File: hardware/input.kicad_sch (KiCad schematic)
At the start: 5 parts, among them J5 Conn_Coaxial

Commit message: FEM v3 Updates
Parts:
- C105: value 100n -> 470n; footprint Capacitor_SMD:C_0402_1005Metric -> Capacitor_SMD:C_0603_1608Metric; LCSC C60474 -> C1623; MPN CC0402KRX7R7BB104 -> CL10B474KA8NNNC
- L25, L6: value 150u -> 47u; footprint Inductor_SMD:L_1812_4532Metric -> Inductor_SMD:L_0603_1608Metric; LCSC C394135 -> C2844630; MPN FHW1812IF151JST -> MLW1608RF-470MT

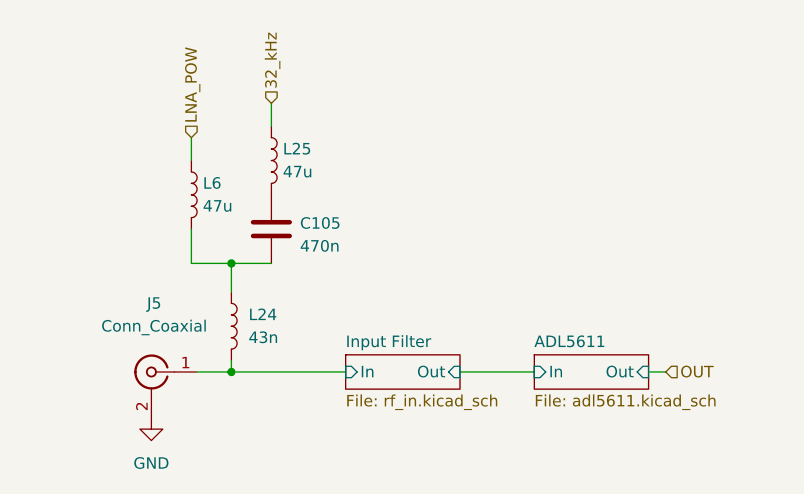
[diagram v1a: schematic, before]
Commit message: Remove cal circuit, swap attens, swap norflash
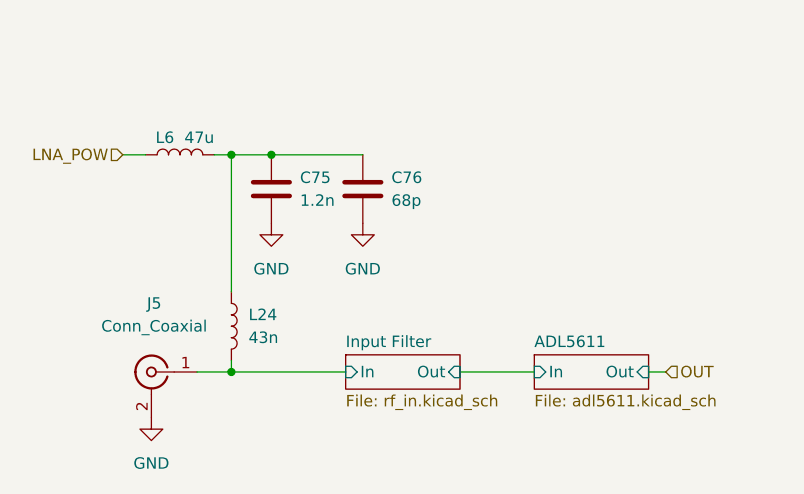
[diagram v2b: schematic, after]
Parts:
- removed C105: 470n, Capacitor_SMD:C_0603_1608Metric, symbol Device:C
- removed L25: 47u, Inductor_SMD:L_0603_1608Metric, symbol Device:L
- added C75: 1.2n, Capacitor_SMD:C_0603_1608Metric, symbol Device:C
- added C76: 68p, Capacitor_SMD:C_0603_1608Metric, symbol Device:C
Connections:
- net GND: now also C75.1, C76.1
- net at L24.1, L6.2: now also C75.2, C76.2
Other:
- moved on the sheet: L6

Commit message: Update FEM hardware design for production version
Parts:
- renumbered J5 to J6, L6 to L22, L24 to L23
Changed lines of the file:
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@@
         )
         (path "/e63e39d7-6ac0-4ffd-8aa3-1841a4541b55/546148dc-8a5c-4178-ace4-1d6889891417/a017f007-4f07-4a1d-ad0a-a026b6928c1c"
-          (reference "#PWR04") (unit 1)
+          (reference "#PWR083") (unit 1)
         )
       )
@@
         )
         (path "/e63e39d7-6ac0-4ffd-8aa3-1841a4541b55/546148dc-8a5c-4178-ace4-1d6889891417/b519df87-7202-4a5b-9b12-1283a4d92d20"
-          (reference "C33") (unit 1)
-        )
-        (path "/e63e39d7-6ac0-4ffd-8aa3-1841a4541b55/546148dc-8a5c-4178-ace4-1d6889891417/a017f007-4f07-4a1d-ad0a-a026b6928c1c"
-          (reference "C102") (unit 1)
+          (reference "C2") (unit 1)
+        )
+        (path "/e63e39d7-6ac0-4ffd-8aa3-1841a4541b55/546148dc-8a5c-4178-ace4-1d6889891417/a017f007-4f07-4a1d-ad0a-a026b6928c1c"
+          (reference "C53") (unit 1)
         )
       )
@@
         )
         (path "/e63e39d7-6ac0-4ffd-8aa3-1841a4541b55/546148dc-8a5c-4178-ace4-1d6889891417/b519df87-7202-4a5b-9b12-1283a4d92d20"
-          (reference "C16") (unit 1)
-        )
-        (path "/e63e39d7-6ac0-4ffd-8aa3-1841a4541b55/546148dc-8a5c-4178-ace4-1d6889891417/a017f007-4f07-4a1d-ad0a-a026b6928c1c"
-          (reference "C101") (unit 1)
+          (reference "C1") (unit 1)
+        )
+        (path "/e63e39d7-6ac0-4ffd-8aa3-1841a4541b55/546148dc-8a5c-4178-ace4-1d6889891417/a017f007-4f07-4a1d-ad0a-a026b6928c1c"
+          (reference "C52") (unit 1)
         )
       )
@@
   (symbol (lib_id "power:GND") (at 100.33 133.35 0) (unit 1)
     (in_bom yes) (on_board yes) (dnp no) (fields_autoplaced)
-    (property "Reference" "#PWR056" (at 100.33 139.7 0)
+    (property "Reference" "#PWR082" (at 100.33 139.7 0)
       (effects (font (size 1.27 1.27)) hide)
     )
@@
       (project "GreX Frontend"
         (path "/e63e39d7-6ac0-4ffd-8aa3-1841a4541b55/546148dc-8a5c-4178-ace4-1d6889891417/a017f007-4f07-4a1d-ad0a-a026b6928c1c"
-          (reference "#PWR056") (unit 1)
+          (reference "#PWR082") (unit 1)
         )
         (path "/e63e39d7-6ac0-4ffd-8aa3-1841a4541b55/546148dc-8a5c-4178-ace4-1d6889891417/b519df87-7202-4a5b-9b12-1283a4d92d20"
@@
   (symbol (lib_id "Device:L") (at 109.22 123.19 0) (unit 1)
     (in_bom yes) (on_board yes) (dnp no) (fields_autoplaced)
-    (property "Reference" "L24" (at 111.125 121.9199 0)
+    (property "Reference" "L23" (at 111.125 121.9199 0)
       (effects (font (size 1.27 1.27)) (justify left))
     )
@@
       (project "GreX Frontend"
         (path "/e63e39d7-6ac0-4ffd-8aa3-1841a4541b55/546148dc-8a5c-4178-ace4-1d6889891417/a017f007-4f07-4a1d-ad0a-a026b6928c1c"
-          (reference "L24") (unit 1)
+          (reference "L23") (unit 1)
         )
         (path "/e63e39d7-6ac0-4ffd-8aa3-1841a4541b55/546148dc-8a5c-4178-ace4-1d6889891417/b519df87-7202-4a5b-9b12-1283a4d92d20"
@@
   (symbol (lib_id "Device:L") (at 103.505 104.14 90) (unit 1)
     (in_bom yes) (on_board yes) (dnp no)
-    (property "Reference" "L6" (at 102.87 102.235 90)
+    (property "Reference" "L22" (at 102.87 102.235 90)
       (effects (font (size 1.27 1.27)) (justify left))
     )
@@
       (project "GreX Frontend"
         (path "/e63e39d7-6ac0-4ffd-8aa3-1841a4541b55/546148dc-8a5c-4178-ace4-1d6889891417/a017f007-4f07-4a1d-ad0a-a026b6928c1c"
-          (reference "L6") (unit 1)
+          (reference "L22") (unit 1)
         )
         (path "/e63e39d7-6ac0-4ffd-8aa3-1841a4541b55/546148dc-8a5c-4178-ace4-1d6889891417/b519df87-7202-4a5b-9b12-1283a4d92d20"
@@
         )
         (path "/e63e39d7-6ac0-4ffd-8aa3-1841a4541b55/546148dc-8a5c-4178-ace4-1d6889891417/a017f007-4f07-4a1d-ad0a-a026b6928c1c"
-          (reference "#PWR05") (unit 1)
+          (reference "#PWR084") (unit 1)
         )
       )
@@
   (symbol (lib_id "Connector:Conn_Coaxial") (at 100.33 128.27 0) (mirror y) (unit 1)
     (in_bom yes) (on_board yes) (dnp no) (fields_autoplaced)
-    (property "Reference" "J5" (at 100.6474 120.65 0)
+    (property "Reference" "J6" (at 100.6474 120.65 0)
       (effects (font (size 1.27 1.27)))
     )
@@
       (project "GreX Frontend"
         (path "/e63e39d7-6ac0-4ffd-8aa3-1841a4541b55/546148dc-8a5c-4178-ace4-1d6889891417/a017f007-4f07-4a1d-ad0a-a026b6928c1c"
-          (reference "J5") (unit 1)
-        )
-        (path "/e63e39d7-6ac0-4ffd-8aa3-1841a4541b55/546148dc-8a5c-4178-ace4-1d6889891417/b519df87-7202-4a5b-9b12-1283a4d92d20"
+          (reference "J6") (unit 1)
+        )
+        (path "/e63e39d7-6ac0-4ffd-8aa3-1841a4541b55/546148dc-8a5c-4178-ace4-1d6889891417/b519df87-7202-4a5b-9b12-1283a4d92d20"
